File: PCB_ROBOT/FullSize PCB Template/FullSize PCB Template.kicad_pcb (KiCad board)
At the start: 2 copper layers, 125 x 125 mm, 4 parts

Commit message: REV 2 - metadata update
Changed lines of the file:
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@@
 		(title "Full Size PCB Template")
 		(date "2024-08-05")
-		(rev "Initial Commit")
+		(rev "2 ")
 		(company "FabRice Team - Campus Fab")
 	)
@@
 		)
 	)
+	(gr_line
+		(start 110 25)
+		(end 110 150)
+		(stroke
+			(width 0.2)
+			(type dash)
+		)
+		(layer "F.SilkS")
+	)
 	(gr_arc

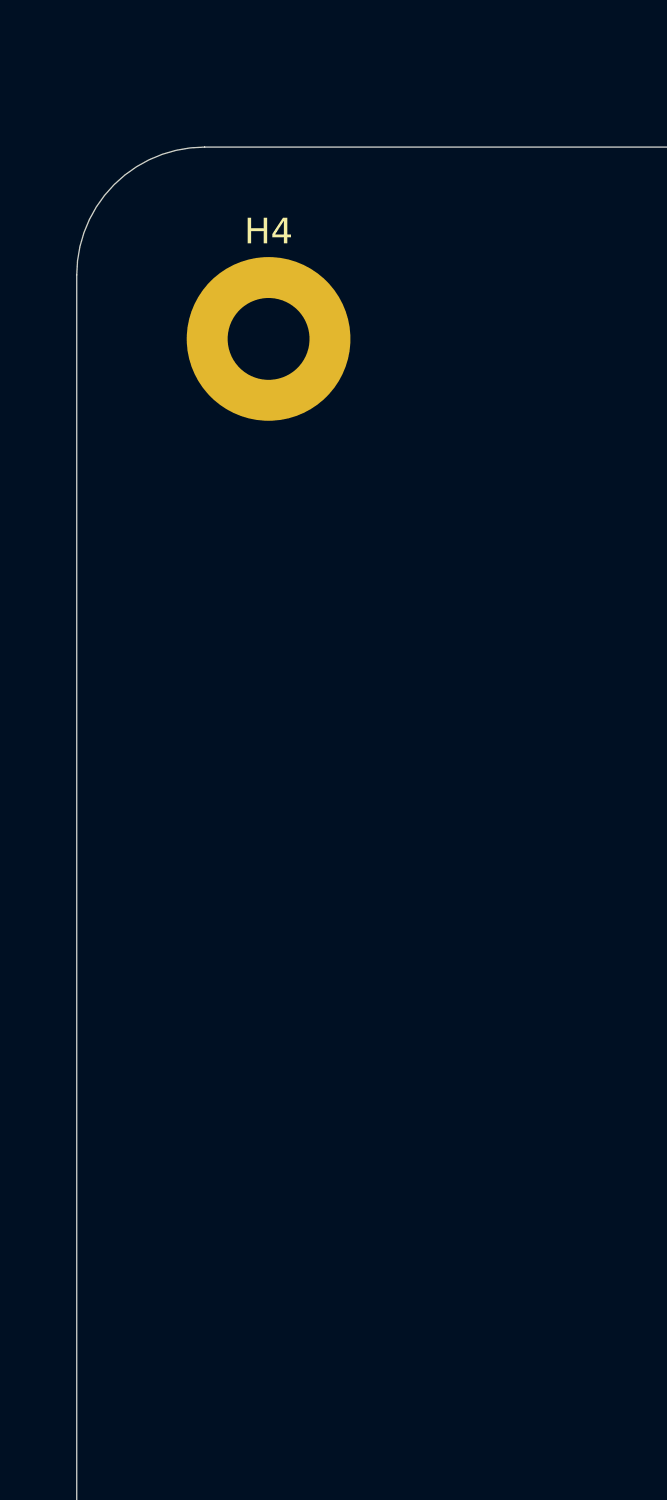
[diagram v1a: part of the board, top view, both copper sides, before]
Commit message: FullSize Template Revision
Adding standard power connector
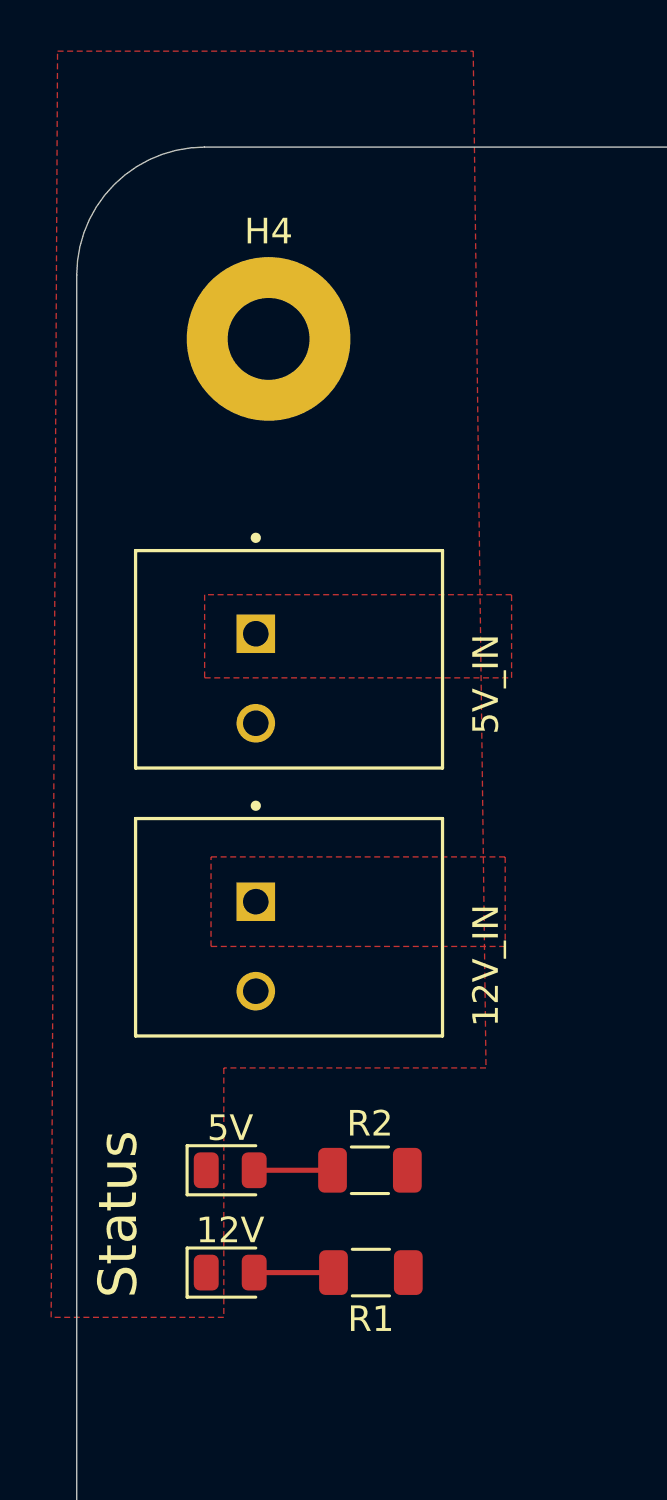
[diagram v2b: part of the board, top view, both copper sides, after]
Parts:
- added 12V: green led, LED_SMD:LED_0805_2012Metric, F.Cu at (41.0, 69.0)
- added 5V: green led, LED_SMD:LED_0805_2012Metric, F.Cu at (41.0, 65.0)
- added J1: 5V_IN, Footprints:PHOENIX_1984963, F.Cu at (37.3, 40.8)
- added J2: 12V_IN, Footprints:PHOENIX_1984963, F.Cu at (37.3, 51.2)
- added R1: 450, Resistor_SMD:R_1206_3216Metric, F.Cu at (46.5, 69.0)
- added R2: 150, Resistor_SMD:R_1206_3216Metric, F.Cu at (46.5, 65.0)
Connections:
- H1 pad 1: unconnected-(H1-Pad1) -> GND
- H2 pad 1: unconnected-(H2-Pad1) -> GND
- H3 pad 1: unconnected-(H3-Pad1) -> GND
- H4 pad 1: unconnected-(H4-Pad1) -> GND
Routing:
- net Net-(D1-A): track 0.00 -> 3.10 mm
- net Net-(D2-A): track 0.00 -> 3.06 mm
- added copper zone on F.Cu, net /12V_LOCAL
- added copper zone on F.Cu, net /5V_LOCAL
- added copper zone on F.Cu, net GND
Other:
- board text added: "Status"

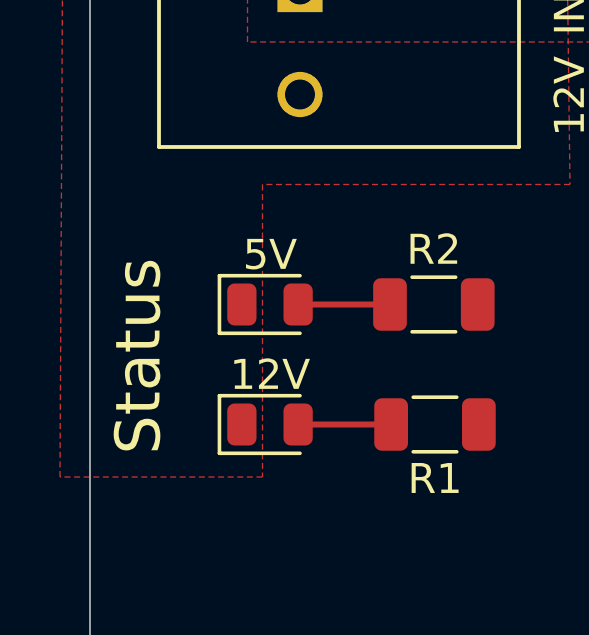
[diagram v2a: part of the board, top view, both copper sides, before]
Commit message: 5v Integration
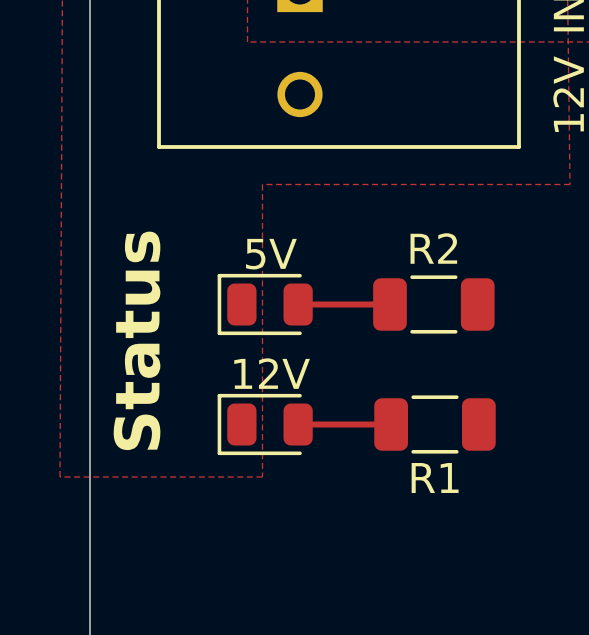
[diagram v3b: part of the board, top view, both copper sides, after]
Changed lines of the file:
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@@
 		)
 		(property "Value" "green led"
-			(at 0 1.65 360)
+			(at 0 1.65 0)
 			(layer "F.Fab")
 			(hide yes)
@@
 		)
 		(fp_text user "${REFERENCE}"
-			(at 0 0 360)
+			(at 0 0 0)
 			(layer "F.Fab")
 			(effects
@@
 		)
 		(property "Value" "green led"
-			(at 0 1.65 360)
+			(at 0 1.65 0)
 			(layer "F.Fab")
 			(hide yes)
@@
 		)
 		(fp_text user "${REFERENCE}"
-			(at 0 0 360)
+			(at 0 0 0)
 			(layer "F.Fab")
 			(effects
@@
 			(font
 				(size 1.5 1.5)
-				(thickness 0.1)
+				(thickness 0.3)
+				(bold yes)
 			)
 			(justify left bottom)
